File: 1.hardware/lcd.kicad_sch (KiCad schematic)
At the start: 40 parts, among them J12 FPC_LCD_40_CONN

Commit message: 오류 일단 다 잡음
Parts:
- C76: footprint Capacitor_SMD:C_0603_1608Metric -> Capacitor_SMD:C_0402_1005Metric
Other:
- moved on the sheet: C76, C77
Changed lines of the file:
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@@
 	)
 	(junction
-		(at 147.32 67.31)
-		(diameter 0)
-		(color 0 0 0 0)
-	)
-	(junction
-		(at 243.84 64.77)
+		(at 245.11 53.34)
 		(diameter 0)
 		(color 0 0 0 0)
 	)
 	(junction
-		(at 261.62 64.77)
+		(at 147.32 67.31)
 		(diameter 0)
 		(color 0 0 0 0)
@@
 	)
 	(junction
-		(at 256.54 64.77)
+		(at 257.81 50.8)
 		(diameter 0)
 		(color 0 0 0 0)
@@
 	(wire
 		(pts
-			(xy 256.54 67.31) (xy 256.54 64.77)
+			(xy 257.81 59.69) (xy 257.81 50.8)
 		)
 		(stroke
@@
 	(wire
 		(pts
+			(xy 245.11 53.34) (xy 265.43 53.34)
+		)
+		(stroke
+			(width 0)
+			(type default)
+		)
+	)
+	(wire
+		(pts
 			(xy 247.65 96.52) (xy 254 96.52)
 		)
@@
 	(wire
 		(pts
-			(xy 243.84 64.77) (xy 256.54 64.77)
+			(xy 238.76 53.34) (xy 245.11 53.34)
 		)
 		(stroke
@@
 	(wire
 		(pts
-			(xy 243.84 72.39) (xy 243.84 73.66)
+			(xy 245.11 64.77) (xy 245.11 66.04)
 		)
 		(stroke
@@
 	(wire
 		(pts
-			(xy 264.16 67.31) (xy 261.62 67.31)
-		)
-		(stroke
-			(width 0)
-			(type default)
-		)
-	)
-	(wire
-		(pts
 			(xy 144.78 77.47) (xy 149.86 77.47)
 		)
@@
 	(wire
 		(pts
-			(xy 243.84 64.77) (xy 243.84 67.31)
-		)
-		(stroke
-			(width 0)
-			(type default)
-		)
-	)
-	(wire
-		(pts
 			(xy 186.69 82.55) (xy 186.69 83.82)
 		)
@@
 	(wire
 		(pts
-			(xy 261.62 64.77) (xy 264.16 64.77)
-		)
-		(stroke
-			(width 0)
-			(type default)
-		)
-	)
-	(wire
-		(pts
 			(xy 299.72 120.65) (xy 304.8 120.65)
 		)
@@
 	(wire
 		(pts
-			(xy 237.49 64.77) (xy 243.84 64.77)
+			(xy 238.76 50.8) (xy 257.81 50.8)
 		)
 		(stroke
@@
 	(wire
 		(pts
-			(xy 256.54 72.39) (xy 256.54 73.66)
-		)
-		(stroke
-			(width 0)
-			(type default)
-		)
-	)
-	(wire
-		(pts
-			(xy 261.62 67.31) (xy 261.62 64.77)
+			(xy 257.81 64.77) (xy 257.81 66.04)
 		)
 		(stroke
@@
 	(wire
 		(pts
-			(xy 256.54 64.77) (xy 261.62 64.77)
+			(xy 257.81 50.8) (xy 265.43 50.8)
 		)
 		(stroke
@@
 	(wire
 		(pts
+			(xy 245.11 53.34) (xy 245.11 59.69)
+		)
+		(stroke
+			(width 0)
+			(type default)
+		)
+	)
+	(wire
+		(pts
 			(xy 137.16 67.31) (xy 137.16 68.58)
 		)
@@
 		)
 	)
+	(global_label "3V3"
+		(shape passive)
+		(at 238.76 53.34 180)
+		(fields_autoplaced yes)
+		(effects
+			(font
+				(size 1.27 1.27)
+			)
+			(justify right)
+		)
+		(property "Intersheetrefs" "${INTERSHEET_REFS}"
+			(at 233.3785 53.34 0)
+			(effects
+				(font
+					(size 1.27 1.27)
+				)
+				(justify right)
+				(hide yes)
+			)
+		)
+	)
 	(global_label "LCD_VCI"
 		(shape passive)
@@
 	(global_label "LCD_VCI"
 		(shape passive)
-		(at 264.16 64.77 0)
+		(at 265.43 50.8 0)
 		(fields_autoplaced yes)
 		(effects
@@
 		)
 		(property "Intersheetrefs" "${INTERSHEET_REFS}"
-			(at 273.533 64.77 0)
+			(at 274.803 50.8 0)
 			(effects
 				(font
@@
 	(global_label "3V3"
 		(shape passive)
-		(at 237.49 64.77 180)
+		(at 238.76 50.8 180)
 		(fields_autoplaced yes)
 		(effects
@@
 		)
 		(property "Intersheetrefs" "${INTERSHEET_REFS}"
-			(at 232.1085 64.77 0)
+			(at 233.3785 50.8 0)
 			(effects
 				(font
@@
 	(global_label "TP_VCI"
 		(shape passive)
-		(at 264.16 67.31 0)
+		(at 265.43 53.34 0)
 		(fields_autoplaced yes)
 		(effects
@@
 		)
 		(property "Intersheetrefs" "${INTERSHEET_REFS}"
-			(at 272.2025 67.31 0)
+			(at 273.4725 53.34 0)
 			(effects
 				(font
@@
 	(symbol
 		(lib_id "power:GND")
-		(at 243.84 73.66 0)
+		(at 245.11 66.04 0)
 		(unit 1)
 		(exclude_from_sim no)
@@
 		(dnp no)
 		(property "Reference" "#PWR0104"
-			(at 243.84 80.01 0)
+			(at 245.11 72.39 0)
 			(effects
 				(font
@@
 		)
 		(property "Value" "GND"
-			(at 243.84 78.232 0)
+			(at 245.11 70.612 0)
 			(effects
 				(font
@@
 		)
 		(property "Footprint" ""
-			(at 243.84 73.66 0)
+			(at 245.11 66.04 0)
 			(effects
 				(font
@@
 		)
 		(property "Datasheet" ""
-			(at 243.84 73.66 0)
+			(at 245.11 66.04 0)
 			(effects
 				(font
@@
 		)
 		(property "Description" "Power symbol creates a global label with name \"GND\" , ground"
-			(at 243.84 73.66 0)
+			(at 245.11 66.04 0)
 			(effects
 				(font
@@
 	(symbol
 		(lib_id "Device:C_Small_US")
-		(at 243.84 69.85 0)
+		(at 245.11 62.23 0)
 		(unit 1)
 		(exclude_from_sim no)
@@
 		(dnp no)
 		(property "Reference" "C76"
-			(at 246.38 68.7069 0)
+			(at 247.65 61.0869 0)
 			(effects
 				(font
@@
 		)
 		(property "Value" "0.1uF/50V"
-			(at 244.094 72.136 0)
+			(at 245.364 64.516 0)
 			(effects
 				(font
@@
 			)
 		)
-		(property "Footprint" "Capacitor_SMD:C_0603_1608Metric"
-			(at 243.84 69.85 0)
+		(property "Footprint" "Capacitor_SMD:C_0402_1005Metric"
+			(at 245.11 62.23 0)
 			(effects
 				(font
@@
 		)
 		(property "Datasheet" ""
-			(at 243.84 69.85 0)
+			(at 245.11 62.23 0)
 			(effects
 				(font
@@
 		)
 		(property "Description" "capacitor, small US symbol"
-			(at 243.84 69.85 0)
+			(at 245.11 62.23 0)
 			(effects
 				(font
@@
 	(symbol
 		(lib_id "power:GND")
-		(at 256.54 73.66 0)
+		(at 257.81 66.04 0)
 		(unit 1)
 		(exclude_from_sim no)
@@
 		(dnp no)
 		(property "Reference" "#PWR0105"
-			(at 256.54 80.01 0)
+			(at 257.81 72.39 0)
 			(effects
 				(font
@@
 		)
 		(property "Value" "GND"
-			(at 256.54 78.232 0)
+			(at 257.81 70.612 0)
 			(effects
 				(font
@@
 		)
 		(property "Footprint" ""
-			(at 256.54 73.66 0)
+			(at 257.81 66.04 0)
 			(effects
 				(font
@@
 		)
 		(property "Datasheet" ""
-			(at 256.54 73.66 0)
+			(at 257.81 66.04 0)
 			(effects
 				(font
@@
 		)
 		(property "Description" "Power symbol creates a global label with name \"GND\" , ground"
-			(at 256.54 73.66 0)
+			(at 257.81 66.04 0)
 			(effects
 				(font
@@
 	(symbol
 		(lib_id "Device:C_Small_US")
-		(at 256.54 69.85 0)
+		(at 257.81 62.23 0)
 		(unit 1)
 		(exclude_from_sim no)
@@
 		(dnp no)
 		(property "Reference" "C77"
-			(at 259.08 68.7069 0)
+			(at 260.35 61.0869 0)
 			(effects
 				(font
@@
 		)
 		(property "Value" "1uF/50V"
-			(at 256.794 72.136 0)
+			(at 258.064 64.516 0)
 			(effects
 				(font
@@
 		)
 		(property "Footprint" "Capacitor_SMD:C_0603_1608Metric"
-			(at 256.54 69.85 0)
+			(at 257.81 62.23 0)
 			(effects
 				(font
@@
 		)
 		(property "Datasheet" ""
-			(at 256.54 69.85 0)
+			(at 257.81 62.23 0)
 			(effects
 				(font
@@
 		)
 		(property "Description" "capacitor, small US symbol"
-			(at 256.54 69.85 0)
+			(at 257.81 62.23 0)
 			(effects
 				(font

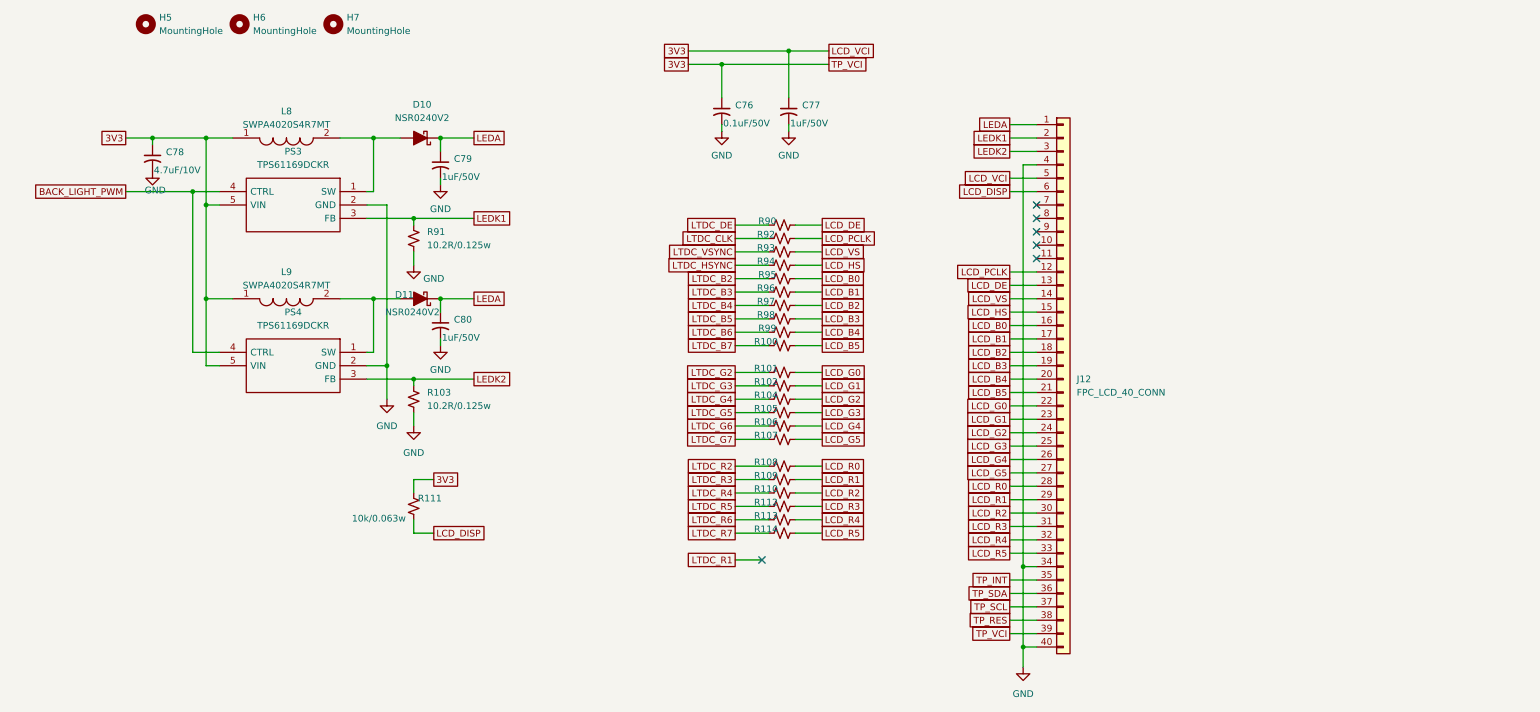
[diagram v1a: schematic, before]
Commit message: 부품 통일 및 필터 부분 캡 선정등 필요해보임
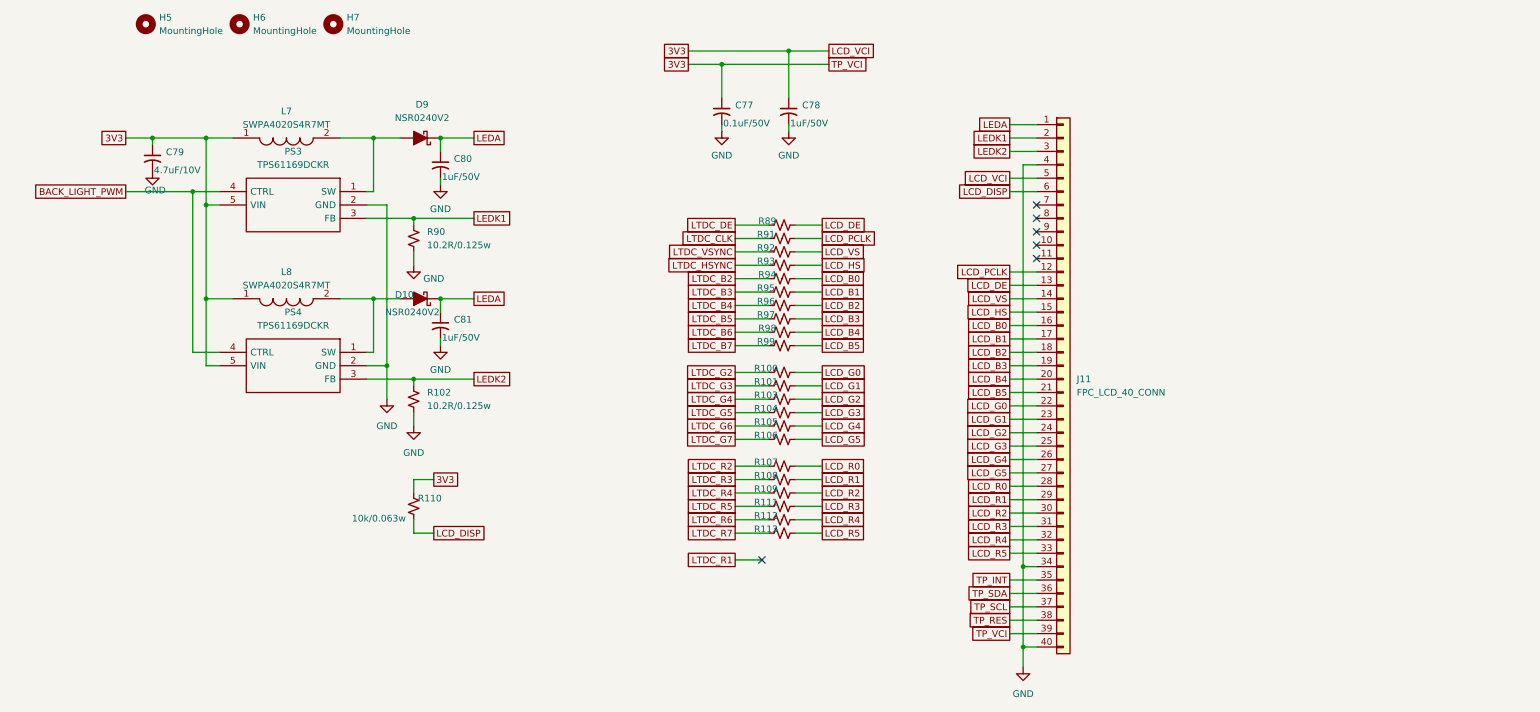
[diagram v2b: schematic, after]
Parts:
- renumbered C76 to C77, C77 to C78, C78 to C79, C79 to C80, C80 to C81, D11 to D10, D10 to D9, J12 to J11, L8 to L7, L9 to L8, R101 to R100, R102 to R101, R103 to R102, R104 to R103, R105 to R104, R106 to R105, R107 to R106, R108 to R107, R109 to R108, R110 to R109, R111 to R110, R112 to R111, R113 to R112, R114 to R113, R90 to R89, R91 to R90, R92 to R91, R93 to R92, R94 to R93, R95 to R94, R96 to R95, R97 to R96, R98 to R97, R99 to R98, R100 to R99

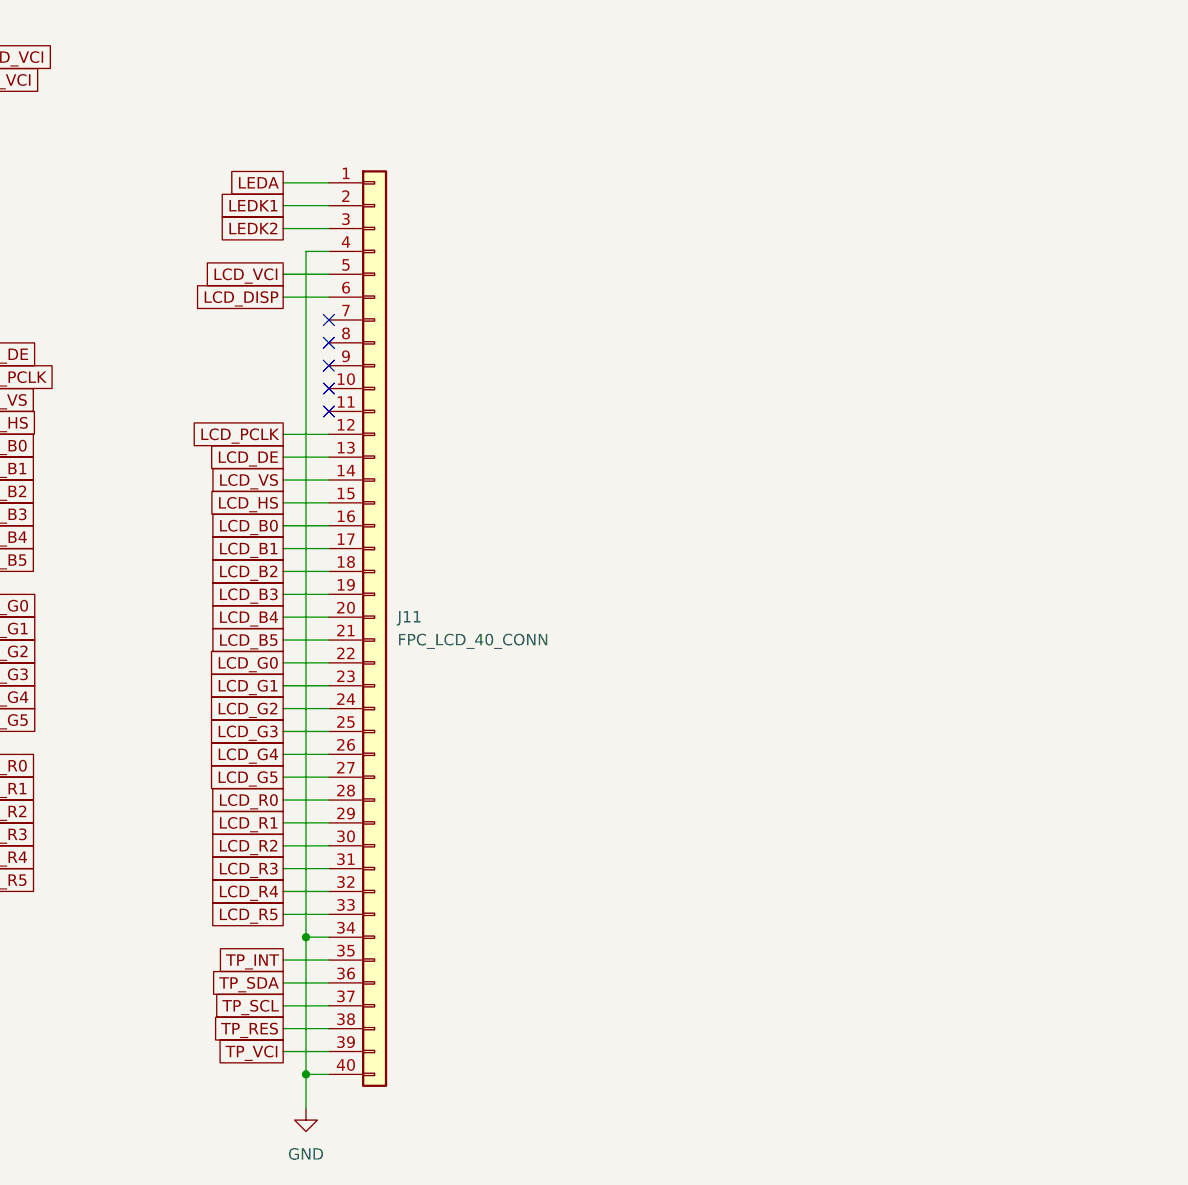
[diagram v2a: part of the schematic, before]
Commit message: 거의 완성 근데 JLC에서 포지션이 좀 개판임
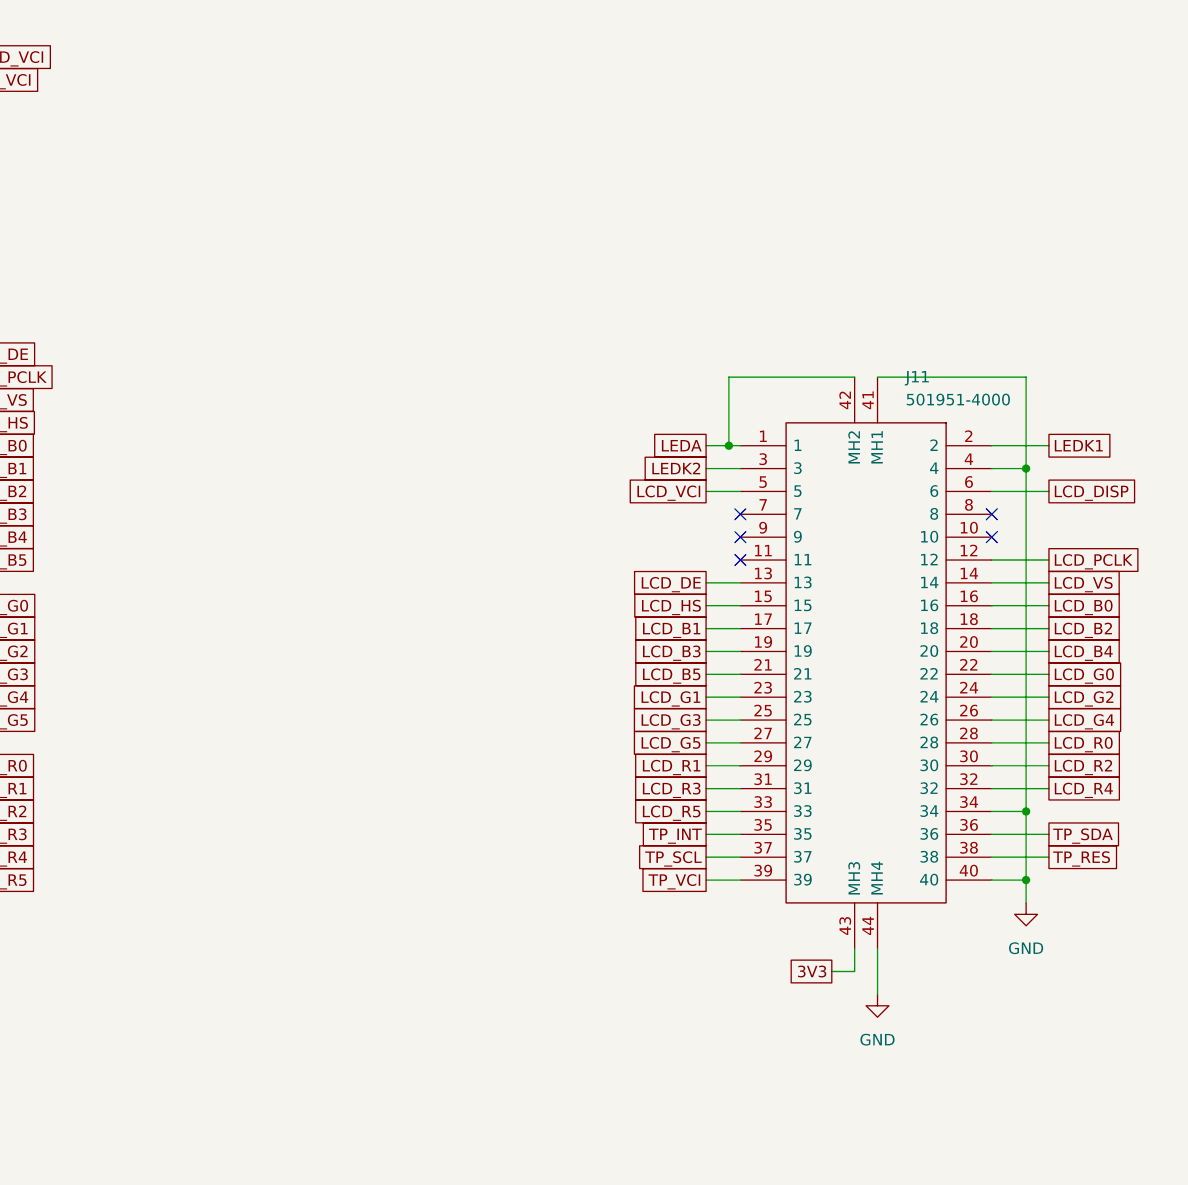
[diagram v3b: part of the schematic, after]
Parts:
- removed J11: FPC_LCD_40_CONN, Connector_FFC-FPC:Amphenol_F32Q-1A7x1-11040_1x40-1MP_P0.5mm_Horizontal, symbol Connector_Generic:Conn_01x40
- added J11: 501951-4000, SamacSys_Parts_Project:5019514000, symbol SamacSys_Parts:501951-4000
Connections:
- net 3V3: now also J11.39, J11.43 (MH3), J11.5
- net GND: now also J11.34, J11.4, J11.40, J11.41 (MH1), J11.44 (MH4)
- net LCD_B0: now also J11.16
- net LCD_B1: now also J11.17
- net LCD_B2: now also J11.18
- net LCD_B3: now also J11.19
- net LCD_B4: now also J11.20
- net LCD_B5: now also J11.21
- net LCD_DE: now also J11.13
- net LCD_DISP: now also J11.6
- net LCD_G0: now also J11.22
- net LCD_G1: now also J11.23
- net LCD_G2: now also J11.24
- net LCD_G3: now also J11.25
- net LCD_G4: now also J11.26
- net LCD_G5: now also J11.27
- net LCD_HS: now also J11.15
- net LCD_PCLK: now also J11.12
- net LCD_R0: now also J11.28
- net LCD_R1: now also J11.29
- net LCD_R2: now also J11.30
- net LCD_R3: now also J11.31
- net LCD_R4: now also J11.32
- net LCD_R5: now also J11.33
- net LCD_VS: now also J11.14
- net LEDA: now also J11.1, J11.42 (MH2)
- net LEDK1: now also J11.2
- net LEDK2: now also J11.3
- net TP_INT: now also J11.35
- net TP_RES: now also J11.38
- net TP_SCL: now also J11.37
- net TP_SDA: now also J11.36
